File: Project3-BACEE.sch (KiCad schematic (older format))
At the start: 12 parts

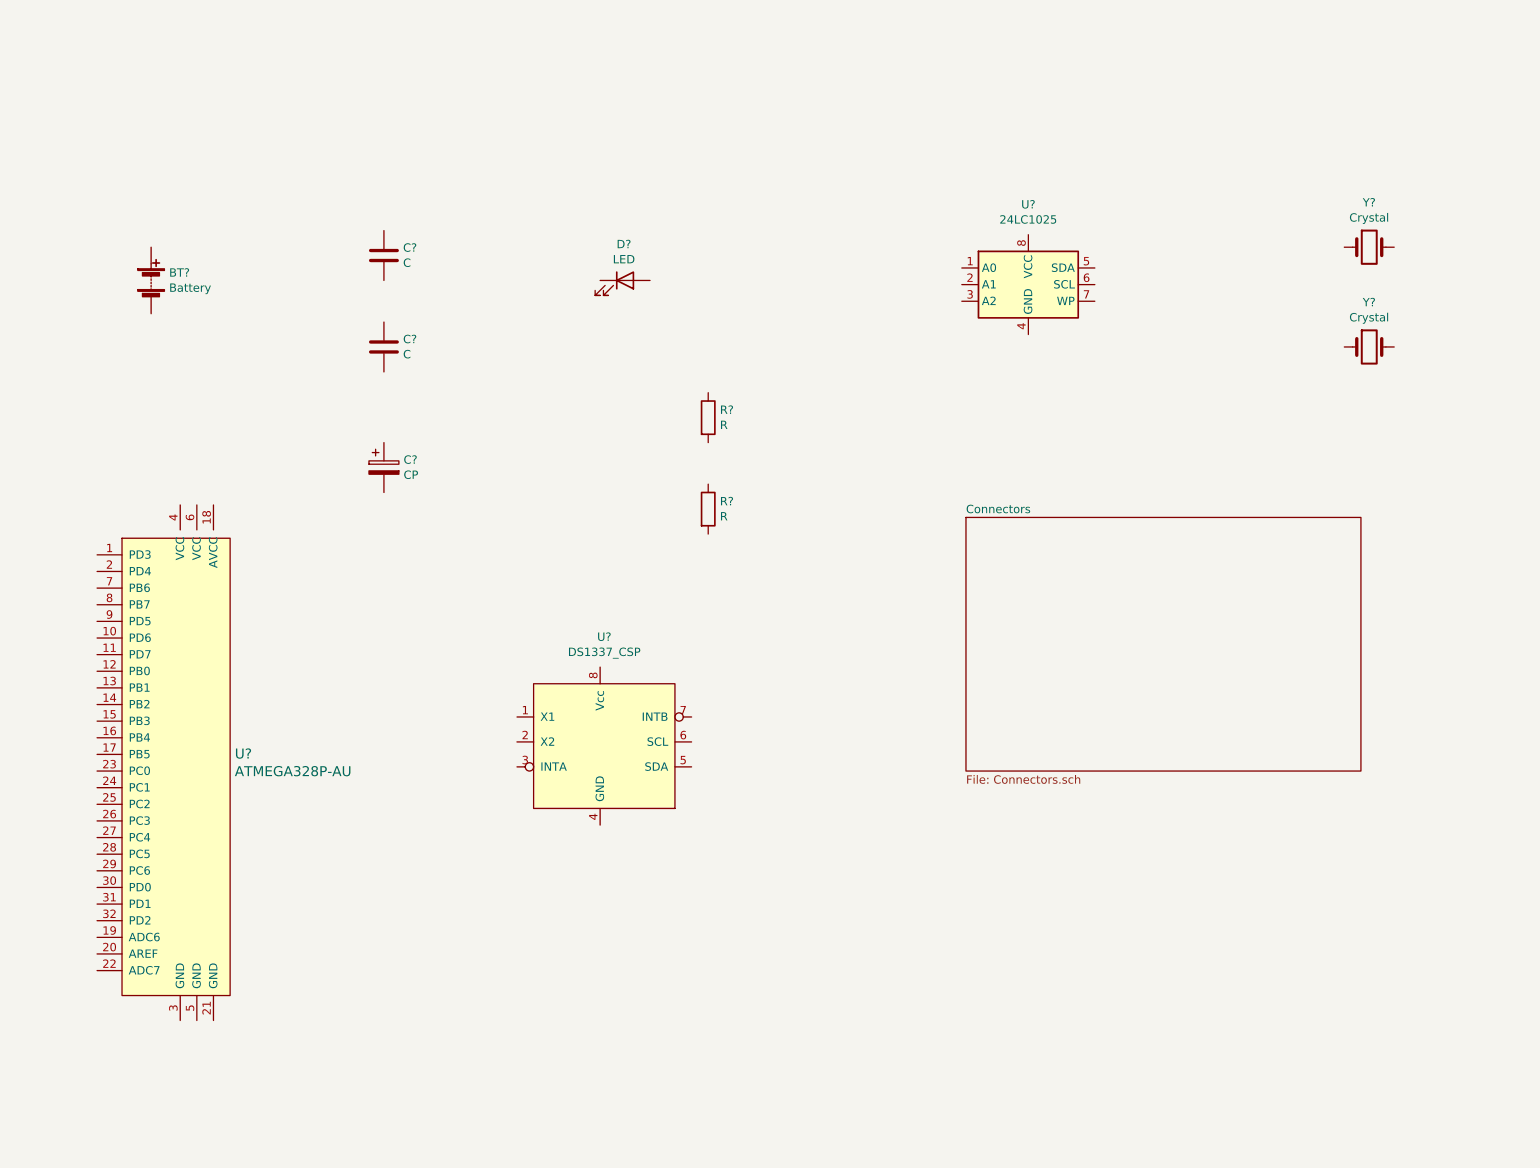
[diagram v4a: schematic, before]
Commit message: annotated symbols
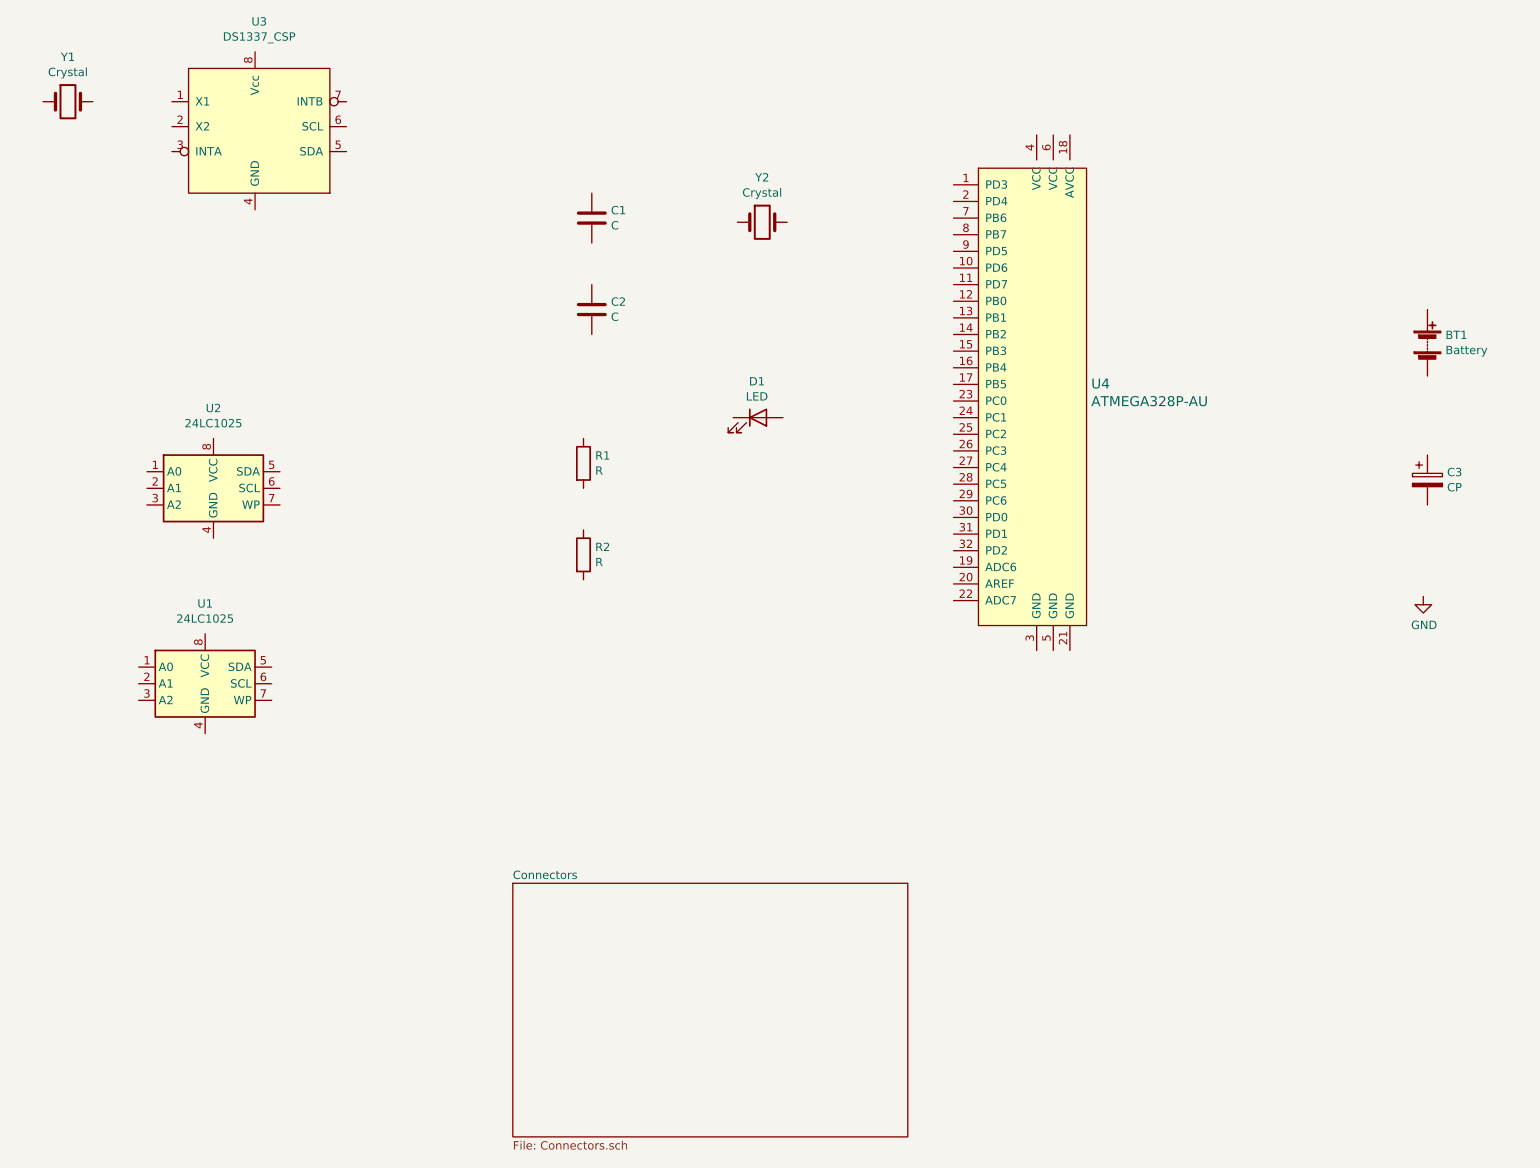
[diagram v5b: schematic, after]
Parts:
- added U1: 24LC1025, symbol Memory_EEPROM:24LC1025
- gave numbers to parts that had none: 12
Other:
- moved on the sheet: BT1, C1, C2, C3, D1, R1, R2, U2, U3, U4, Y1, Y2
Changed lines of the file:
@@
 $EndDescr
 $Comp
-L Device:Battery BT?
+L Device:Battery BT1
 U 1 1 61A18C0A
-P 2275 2500
-F 0 "BT?" H 2383 2546 50  0000 L CNN
-F 1 "Battery" H 2383 2455 50  0000 L CNN
-F 2 "" V 2275 2560 50  0001 C CNN
-F 3 "~" V 2275 2560 50  0001 C CNN
-	1    2275 2500
+P 9950 2875
+F 0 "BT1" H 10058 2921 50  0000 L CNN
+F 1 "Battery" H 10058 2830 50  0000 L CNN
+F 2 "" V 9950 2935 50  0001 C CNN
+F 3 "~" V 9950 2935 50  0001 C CNN
+	1    9950 2875
 	1    0    0    -1
 $EndComp
 $Comp
-L Device:C C?
+L Device:C C1
 U 1 1 61A19A4D
-P 3675 2350
-F 0 "C?" H 3790 2396 50  0000 L CNN
-F 1 "C" H 3790 2305 50  0000 L CNN
-F 2 "" H 3713 2200 50  0001 C CNN
-F 3 "~" H 3675 2350 50  0001 C CNN
-	1    3675 2350
+P 4925 2125
+F 0 "C1" H 5040 2171 50  0000 L CNN
+F 1 "C" H 5040 2080 50  0000 L CNN
+F 2 "" H 4963 1975 50  0001 C CNN
+F 3 "~" H 4925 2125 50  0001 C CNN
+	1    4925 2125
 	1    0    0    -1
 $EndComp
 $Comp
-L Device:C C?
+L Device:C C2
 U 1 1 61A1A1BD
-P 3675 2900
-F 0 "C?" H 3790 2946 50  0000 L CNN
-F 1 "C" H 3790 2855 50  0000 L CNN
-F 2 "" H 3713 2750 50  0001 C CNN
-F 3 "~" H 3675 2900 50  0001 C CNN
-	1    3675 2900
+P 4925 2675
+F 0 "C2" H 5040 2721 50  0000 L CNN
+F 1 "C" H 5040 2630 50  0000 L CNN
+F 2 "" H 4963 2525 50  0001 C CNN
+F 3 "~" H 4925 2675 50  0001 C CNN
+	1    4925 2675
 	1    0    0    -1
 $EndComp
 $Comp
-L Device:CP C?
+L Device:CP C3
 U 1 1 61A1ACBD
-P 3675 3625
-F 0 "C?" H 3793 3671 50  0000 L CNN
-F 1 "CP" H 3793 3580 50  0000 L CNN
-F 2 "" H 3713 3475 50  0001 C CNN
-F 3 "~" H 3675 3625 50  0001 C CNN
-	1    3675 3625
+P 9950 3700
+F 0 "C3" H 10068 3746 50  0000 L CNN
+F 1 "CP" H 10068 3655 50  0000 L CNN
+F 2 "" H 9988 3550 50  0001 C CNN
+F 3 "~" H 9950 3700 50  0001 C CNN
+	1    9950 3700
 	1    0    0    -1
 $EndComp
 $Comp
-L Device:LED D?
+L Device:LED D1
 U 1 1 61A1B764
-P 5125 2500
-F 0 "D?" H 5118 2717 50  0000 C CNN
-F 1 "LED" H 5118 2626 50  0000 C CNN
-F 2 "" H 5125 2500 50  0001 C CNN
-F 3 "~" H 5125 2500 50  0001 C CNN
-	1    5125 2500
+P 5925 3325
+F 0 "D1" H 5918 3542 50  0000 C CNN
+F 1 "LED" H 5918 3451 50  0000 C CNN
+F 2 "" H 5925 3325 50  0001 C CNN
+F 3 "~" H 5925 3325 50  0001 C CNN
+	1    5925 3325
 	1    0    0    -1
 $EndComp
 $Comp
-L Device:R R?
+L Device:R R1
 U 1 1 61A1BA7E
-P 5625 3325
-F 0 "R?" H 5695 3371 50  0000 L CNN
-F 1 "R" H 5695 3280 50  0000 L CNN
-F 2 "" V 5555 3325 50  0001 C CNN
-F 3 "~" H 5625 3325 50  0001 C CNN
-	1    5625 3325
+P 4875 3600
+F 0 "R1" H 4945 3646 50  0000 L CNN
+F 1 "R" H 4945 3555 50  0000 L CNN
+F 2 "" V 4805 3600 50  0001 C CNN
+F 3 "~" H 4875 3600 50  0001 C CNN
+	1    4875 3600
 	1    0    0    -1
 $EndComp
 $Comp
-L Device:R R?
+L Device:R R2
 U 1 1 61A1C043
-P 5625 3875
-F 0 "R?" H 5695 3921 50  0000 L CNN
-F 1 "R" H 5695 3830 50  0000 L CNN
-F 2 "" V 5555 3875 50  0001 C CNN
-F 3 "~" H 5625 3875 50  0001 C CNN
-	1    5625 3875
+P 4875 4150
+F 0 "R2" H 4945 4196 50  0000 L CNN
+F 1 "R" H 4945 4105 50  0000 L CNN
+F 2 "" V 4805 4150 50  0001 C CNN
+F 3 "~" H 4875 4150 50  0001 C CNN
+	1    4875 4150
 	1    0    0    -1
 $EndComp
 $Comp
-L Memory_EEPROM:24LC1025 U?
+L Memory_EEPROM:24LC1025 U2
 U 1 1 61A1CEED
-P 7550 2525
-F 0 "U?" H 7550 3006 50  0000 C CNN
-F 1 "24LC1025" H 7550 2915 50  0000 C CNN
-F 2 "" H 7550 2525 50  0001 C CNN
-F 3 "http://ww1.microchip.com/downloads/en/DeviceDoc/21941B.pdf" H 7550 2525 50  0001 C CNN
-	1    7550 2525
+P 2650 3750
+F 0 "U2" H 2650 4231 50  0000 C CNN
+F 1 "24LC1025" H 2650 4140 50  0000 C CNN
+F 2 "" H 2650 3750 50  0001 C CNN
+F 3 "http://ww1.microchip.com/downloads/en/DeviceDoc/21941B.pdf" H 2650 3750 50  0001 C CNN
+	1    2650 3750
 	1    0    0    -1
 $EndComp
 $Sheet
-S 7175 3925 2375 1525
+S 4450 6125 2375 1525
 U 61A1FED7
 F0 "Connectors" 50
@@
 $EndSheet
 $Comp
-L dk_Embedded-Microcontrollers:ATMEGA328P-AU U?
+L dk_Embedded-Microcontrollers:ATMEGA328P-AU U4
 U 1 1 61A26237
-P 2450 5450
-F 0 "U?" H 2778 5553 60  0000 L CNN
-F 1 "ATMEGA328P-AU" H 2778 5447 60  0000 L CNN
-F 2 "digikey-footprints:TQFP-32_7x7mm" H 2650 5650 60  0001 L CNN
-F 3 "http://www.microchip.com/mymicrochip/filehandler.aspx?ddocname=en608326" H 2650 5750 60  0001 L CNN
-F 4 "ATMEGA328P-AU-ND" H 2650 5850 60  0001 L CNN "Digi-Key_PN"
-F 5 "ATMEGA328P-AU" H 2650 5950 60  0001 L CNN "MPN"
-F 6 "Integrated Circuits (ICs)" H 2650 6050 60  0001 L CNN "Category"
-F 7 "Embedded - Microcontrollers" H 2650 6150 60  0001 L CNN "Family"
-F 8 "http://www.microchip.com/mymicrochip/filehandler.aspx?ddocname=en608326" H 2650 6250 60  0001 L CNN "DK_Datasheet_Link"
-F 9 "/product-detail/en/microchip-technology/ATMEGA328P-AU/ATMEGA328P-AU-ND/1832260" H 2650 6350 60  0001 L CNN "DK_Detail_Page"
-F 10 "IC MCU 8BIT 32KB FLASH 32TQFP" H 2650 6450 60  0001 L CNN "Description"
-F 11 "Microchip Technology" H 2650 6550 60  0001 L CNN "Manufacturer"
-F 12 "Active" H 2650 6650 60  0001 L CNN "Status"
-	1    2450 5450
+P 7600 3225
+F 0 "U4" H 7928 3328 60  0000 L CNN
+F 1 "ATMEGA328P-AU" H 7928 3222 60  0000 L CNN
+F 2 "digikey-footprints:TQFP-32_7x7mm" H 7800 3425 60  0001 L CNN
+F 3 "http://www.microchip.com/mymicrochip/filehandler.aspx?ddocname=en608326" H 7800 3525 60  0001 L CNN
+F 4 "ATMEGA328P-AU-ND" H 7800 3625 60  0001 L CNN "Digi-Key_PN"
+F 5 "ATMEGA328P-AU" H 7800 3725 60  0001 L CNN "MPN"
+F 6 "Integrated Circuits (ICs)" H 7800 3825 60  0001 L CNN "Category"
+F 7 "Embedded - Microcontrollers" H 7800 3925 60  0001 L CNN "Family"
+F 8 "http://www.microchip.com/mymicrochip/filehandler.aspx?ddocname=en608326" H 7800 4025 60  0001 L CNN "DK_Datasheet_Link"
+F 9 "/product-detail/en/microchip-technology/ATMEGA328P-AU/ATMEGA328P-AU-ND/1832260" H 7800 4125 60  0001 L CNN "DK_Detail_Page"
+F 10 "IC MCU 8BIT 32KB FLASH 32TQFP" H 7800 4225 60  0001 L CNN "Description"
+F 11 "Microchip Technology" H 7800 4325 60  0001 L CNN "Manufacturer"
+F 12 "Active" H 7800 4425 60  0001 L CNN "Status"
+	1    7600 3225
 	1    0    0    -1
 $EndComp
 $Comp
-L project3:DS1337_CSP U?
+L project3:DS1337_CSP U3
 U 1 1 61A2C2A1
-P 4975 5175
-F 0 "U?" H 5000 5706 50  0000 C CNN
-F 1 "DS1337_CSP" H 5000 5615 50  0000 C CNN
-F 2 "" H 4975 5975 50  0001 C CNN
-F 3 "" H 4975 5975 50  0001 C CNN
-	1    4975 5175
+P 2900 1475
+F 0 "U3" H 2925 2006 50  0000 C CNN
+F 1 "DS1337_CSP" H 2925 1915 50  0000 C CNN
+F 2 "" H 2900 2275 50  0001 C CNN
+F 3 "" H 2900 2275 50  0001 C CNN
+	1    2900 1475
 	1    0    0    -1
 $EndComp
 $Comp
-L Device:Crystal Y?
+L Device:Crystal Y1
 U 1 1 61A2DC0F
-P 9600 2300
-F 0 "Y?" H 9600 2568 50  0000 C CNN
-F 1 "Crystal" H 9600 2477 50  0000 C CNN
-F 2 "" H 9600 2300 50  0001 C CNN
-F 3 "~" H 9600 2300 50  0001 C CNN
-	1    9600 2300
+P 1775 1425
+F 0 "Y1" H 1775 1693 50  0000 C CNN
+F 1 "Crystal" H 1775 1602 50  0000 C CNN
+F 2 "" H 1775 1425 50  0001 C CNN
+F 3 "~" H 1775 1425 50  0001 C CNN
+	1    1775 1425
 	1    0    0    -1
 $EndComp
 $Comp
-L Device:Crystal Y?
+L Device:Crystal Y2
 U 1 1 61A2E8DA
-P 9600 2900
-F 0 "Y?" H 9600 3168 50  0000 C CNN
-F 1 "Crystal" H 9600 3077 50  0000 C CNN
-F 2 "" H 9600 2900 50  0001 C CNN
-F 3 "~" H 9600 2900 50  0001 C CNN
-	1    9600 2900
+P 5950 2150
+F 0 "Y2" H 5950 2418 50  0000 C CNN
+F 1 "Crystal" H 5950 2327 50  0000 C CNN
+F 2 "" H 5950 2150 50  0001 C CNN
+F 3 "~" H 5950 2150 50  0001 C CNN
+	1    5950 2150
 	1    0    0    -1
 $EndComp
+$Comp
+L Memory_EEPROM:24LC1025 U1
+U 1 1 61A70DAE
+P 2600 4925
+F 0 "U1" H 2600 5406 50  0000 C CNN
+F 1 "24LC1025" H 2600 5315 50  0000 C CNN
+F 2 "" H 2600 4925 50  0001 C CNN
+F 3 "http://ww1.microchip.com/downloads/en/DeviceDoc/21941B.pdf" H 2600 4925 50  0001 C CNN
+	1    2600 4925
+	1    0    0    -1
+$EndComp
+$Comp
+L power:GND #PWR01
+U 1 1 61A728B0
+P 9925 4400
+F 0 "#PWR01" H 9925 4150 50  0001 C CNN
+F 1 "GND" H 9930 4227 50  0000 C CNN
+F 2 "" H 9925 4400 50  0001 C CNN
+F 3 "" H 9925 4400 50  0001 C CNN
+	1    9925 4400
+	1    0    0    -1
+$EndComp

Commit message: save footprint associations
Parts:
- BT1: footprint (none) -> Connector_PinHeader_2.54mm:PinHeader_1x02_P2.54mm_Vertical
- C1, C2, C3: footprint (none) -> Capacitor_SMD:C_0805_2012Metric_Pad1.18x1.45mm_HandSolder
- D1: footprint (none) -> LED_SMD:LED_0805_2012Metric_Pad1.15x1.40mm_HandSolder
- R1, R2: footprint (none) -> Resistor_SMD:R_0805_2012Metric_Pad1.20x1.40mm_HandSolder
- U1, U2: footprint (none) -> Package_SO:SOIJ-8_5.3x5.3mm_P1.27mm
- U3: footprint (none) -> Package_SO:SO-8_5.3x6.2mm_P1.27mm
- Y1: footprint (none) -> Crystal:Crystal_SMD_MicroCrystal_CC7V-T1A-2Pin_3.2x1.5mm
- Y2: footprint (none) -> Crystal:Crystal_SMD_5032-2Pin_5.0x3.2mm_HandSoldering
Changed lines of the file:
@@
 F 0 "BT1" H 10058 2921 50  0000 L CNN
 F 1 "Battery" H 10058 2830 50  0000 L CNN
-F 2 "" V 9950 2935 50  0001 C CNN
+F 2 "Connector_PinHeader_2.54mm:PinHeader_1x02_P2.54mm_Vertical" V 9950 2935 50  0001 C CNN
 F 3 "~" V 9950 2935 50  0001 C CNN
 	1    9950 2875
@@
 F 0 "C1" H 5040 2171 50  0000 L CNN
 F 1 "C" H 5040 2080 50  0000 L CNN
-F 2 "" H 4963 1975 50  0001 C CNN
+F 2 "Capacitor_SMD:C_0805_2012Metric_Pad1.18x1.45mm_HandSolder" H 4963 1975 50  0001 C CNN
 F 3 "~" H 4925 2125 50  0001 C CNN
 	1    4925 2125
@@
 F 0 "C2" H 5040 2721 50  0000 L CNN
 F 1 "C" H 5040 2630 50  0000 L CNN
-F 2 "" H 4963 2525 50  0001 C CNN
+F 2 "Capacitor_SMD:C_0805_2012Metric_Pad1.18x1.45mm_HandSolder" H 4963 2525 50  0001 C CNN
 F 3 "~" H 4925 2675 50  0001 C CNN
 	1    4925 2675
@@
 F 0 "C3" H 10068 3746 50  0000 L CNN
 F 1 "CP" H 10068 3655 50  0000 L CNN
-F 2 "" H 9988 3550 50  0001 C CNN
+F 2 "Capacitor_SMD:C_0805_2012Metric_Pad1.18x1.45mm_HandSolder" H 9988 3550 50  0001 C CNN
 F 3 "~" H 9950 3700 50  0001 C CNN
 	1    9950 3700
@@
 F 0 "D1" H 5918 3542 50  0000 C CNN
 F 1 "LED" H 5918 3451 50  0000 C CNN
-F 2 "" H 5925 3325 50  0001 C CNN
+F 2 "LED_SMD:LED_0805_2012Metric_Pad1.15x1.40mm_HandSolder" H 5925 3325 50  0001 C CNN
 F 3 "~" H 5925 3325 50  0001 C CNN
 	1    5925 3325
@@
 F 0 "R1" H 4945 3646 50  0000 L CNN
 F 1 "R" H 4945 3555 50  0000 L CNN
-F 2 "" V 4805 3600 50  0001 C CNN
+F 2 "Resistor_SMD:R_0805_2012Metric_Pad1.20x1.40mm_HandSolder" V 4805 3600 50  0001 C CNN
 F 3 "~" H 4875 3600 50  0001 C CNN
 	1    4875 3600
@@
 F 0 "R2" H 4945 4196 50  0000 L CNN
 F 1 "R" H 4945 4105 50  0000 L CNN
-F 2 "" V 4805 4150 50  0001 C CNN
+F 2 "Resistor_SMD:R_0805_2012Metric_Pad1.20x1.40mm_HandSolder" V 4805 4150 50  0001 C CNN
 F 3 "~" H 4875 4150 50  0001 C CNN
 	1    4875 4150
@@
 F 0 "U2" H 2650 4231 50  0000 C CNN
 F 1 "24LC1025" H 2650 4140 50  0000 C CNN
-F 2 "" H 2650 3750 50  0001 C CNN
+F 2 "Package_SO:SOIJ-8_5.3x5.3mm_P1.27mm" H 2650 3750 50  0001 C CNN
 F 3 "http://ww1.microchip.com/downloads/en/DeviceDoc/21941B.pdf" H 2650 3750 50  0001 C CNN
 	1    2650 3750
@@
 F 0 "U3" H 2925 2006 50  0000 C CNN
 F 1 "DS1337_CSP" H 2925 1915 50  0000 C CNN
-F 2 "" H 2900 2275 50  0001 C CNN
+F 2 "Package_SO:SO-8_5.3x6.2mm_P1.27mm" H 2900 2275 50  0001 C CNN
 F 3 "" H 2900 2275 50  0001 C CNN
 	1    2900 1475
@@
 F 0 "Y1" H 1775 1693 50  0000 C CNN
 F 1 "Crystal" H 1775 1602 50  0000 C CNN
-F 2 "" H 1775 1425 50  0001 C CNN
+F 2 "Crystal:Crystal_SMD_MicroCrystal_CC7V-T1A-2Pin_3.2x1.5mm" H 1775 1425 50  0001 C CNN
 F 3 "~" H 1775 1425 50  0001 C CNN
 	1    1775 1425
@@
 F 0 "Y2" H 5950 2418 50  0000 C CNN
 F 1 "Crystal" H 5950 2327 50  0000 C CNN
-F 2 "" H 5950 2150 50  0001 C CNN
+F 2 "Crystal:Crystal_SMD_5032-2Pin_5.0x3.2mm_HandSoldering" H 5950 2150 50  0001 C CNN
 F 3 "~" H 5950 2150 50  0001 C CNN
 	1    5950 2150
@@
 F 0 "U1" H 2600 5406 50  0000 C CNN
 F 1 "24LC1025" H 2600 5315 50  0000 C CNN
-F 2 "" H 2600 4925 50  0001 C CNN
+F 2 "Package_SO:SOIJ-8_5.3x5.3mm_P1.27mm" H 2600 4925 50  0001 C CNN
 F 3 "http://ww1.microchip.com/downloads/en/DeviceDoc/21941B.pdf" H 2600 4925 50  0001 C CNN
 	1    2600 4925

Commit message: save footprint associations
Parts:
- BT1: value Battery -> Battery 3V
- C1, C2: value C -> 22pF
- C3: value CP -> 10uF
- R1: value R -> 330ohm
- R2: value R -> 10kohm
- Y1: value Crystal -> Crystal 32MHz
- Y2: value Crystal -> Crystal 16MHz
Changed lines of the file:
@@
 P 9950 2875
 F 0 "BT1" H 10058 2921 50  0000 L CNN
-F 1 "Battery" H 10058 2830 50  0000 L CNN
+F 1 "Battery 3V" H 10058 2830 50  0000 L CNN
 F 2 "Connector_PinHeader_2.54mm:PinHeader_1x02_P2.54mm_Vertical" V 9950 2935 50  0001 C CNN
 F 3 "~" V 9950 2935 50  0001 C CNN
@@
 P 4925 2125
 F 0 "C1" H 5040 2171 50  0000 L CNN
-F 1 "C" H 5040 2080 50  0000 L CNN
+F 1 "22pF" H 5040 2080 50  0000 L CNN
 F 2 "Capacitor_SMD:C_0805_2012Metric_Pad1.18x1.45mm_HandSolder" H 4963 1975 50  0001 C CNN
 F 3 "~" H 4925 2125 50  0001 C CNN
@@
 P 4925 2675
 F 0 "C2" H 5040 2721 50  0000 L CNN
-F 1 "C" H 5040 2630 50  0000 L CNN
+F 1 "22pF" H 5040 2630 50  0000 L CNN
 F 2 "Capacitor_SMD:C_0805_2012Metric_Pad1.18x1.45mm_HandSolder" H 4963 2525 50  0001 C CNN
 F 3 "~" H 4925 2675 50  0001 C CNN
@@
 P 9950 3700
 F 0 "C3" H 10068 3746 50  0000 L CNN
-F 1 "CP" H 10068 3655 50  0000 L CNN
+F 1 "10uF" H 10068 3655 50  0000 L CNN
 F 2 "Capacitor_SMD:C_0805_2012Metric_Pad1.18x1.45mm_HandSolder" H 9988 3550 50  0001 C CNN
 F 3 "~" H 9950 3700 50  0001 C CNN
@@
 P 4875 3600
 F 0 "R1" H 4945 3646 50  0000 L CNN
-F 1 "R" H 4945 3555 50  0000 L CNN
+F 1 "330ohm" H 4945 3555 50  0000 L CNN
 F 2 "Resistor_SMD:R_0805_2012Metric_Pad1.20x1.40mm_HandSolder" V 4805 3600 50  0001 C CNN
 F 3 "~" H 4875 3600 50  0001 C CNN
@@
 P 4875 4150
 F 0 "R2" H 4945 4196 50  0000 L CNN
-F 1 "R" H 4945 4105 50  0000 L CNN
+F 1 "10kohm" H 4945 4105 50  0000 L CNN
 F 2 "Resistor_SMD:R_0805_2012Metric_Pad1.20x1.40mm_HandSolder" V 4805 4150 50  0001 C CNN
 F 3 "~" H 4875 4150 50  0001 C CNN
@@
 P 1775 1425
 F 0 "Y1" H 1775 1693 50  0000 C CNN
-F 1 "Crystal" H 1775 1602 50  0000 C CNN
+F 1 "Crystal 32MHz" H 1775 1602 50  0000 C CNN
 F 2 "Crystal:Crystal_SMD_MicroCrystal_CC7V-T1A-2Pin_3.2x1.5mm" H 1775 1425 50  0001 C CNN
 F 3 "~" H 1775 1425 50  0001 C CNN
@@
 P 5950 2150
 F 0 "Y2" H 5950 2418 50  0000 C CNN
-F 1 "Crystal" H 5950 2327 50  0000 C CNN
+F 1 "Crystal 16MHz" H 5950 2327 50  0000 C CNN
 F 2 "Crystal:Crystal_SMD_5032-2Pin_5.0x3.2mm_HandSoldering" H 5950 2150 50  0001 C CNN
 F 3 "~" H 5950 2150 50  0001 C CNN
